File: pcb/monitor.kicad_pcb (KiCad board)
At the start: 4 copper layers, 100 x 100 mm, 146 parts, among them K101 DG128-02P, K102 DG128-02P, K103 DG128-02P, K104 DG128-02P, K105 DG128-02P, K106 DG128-02P, K107 DG128-02P, K108 DG128-02P, K109 DG128-02P, K110 DG128-02P, K111 DG128-02P, K112 DG128-02P, K113 JUMPER_3, K114 JUMPER_3, K3 DG128-02P, K4 DG128-02P, K401 DG128-02P, K402 DG128-02P, K403 DG128-02P, K5 DG128-02P, K6 DG128-02P, K7 CONNECT_2, K8 CONNECT_2, T201 ZUMT718, T202 ZUMT718, T203 ZUMT718, T204 ZUMT718, T205 ZUMT718, T206 ZUMT718, T207 ZUMT718, T208 ZUMT718, T209 ZUMT718, T210 ZUMT718, T211 ZUMT718, T212 ZUMT718, U1 LTC6803-3, U401 ADUM5401

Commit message: Battery connections
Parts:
- moved R219 184.9 mm to (147.3, 111.8), turned to 270 degrees
- moved LD209 181.9 mm to (147.3, 106.7), turned to 180 degrees
- moved T209 178.8 mm to (143.5, 106.7), turned to 270 degrees
- moved D311 177.6 mm to (144.8, 102.9)
- moved R216 176.9 mm to (137.2, 111.8), turned to 270 degrees
- moved R217 176.8 mm to (147.3, 97.8), turned to 270 degrees
- moved LD208 173.8 mm to (137.2, 106.7), turned to 180 degrees
- moved C311 172.6 mm to (142.2, 97.8), turned to 270 degrees
- moved T208 170.8 mm to (133.3, 106.7), turned to 270 degrees
- moved D310 169.4 mm to (134.6, 102.9)
- moved R214 168.5 mm to (137.2, 97.8), turned to 270 degrees
- moved C310 164.3 mm to (132.1, 97.8), turned to 270 degrees
- moved R221 143.6 mm to (111.8, 90.2), turned to 180 degrees
- moved C306 140.5 mm to (111.8, 85.1), turned to 180 degrees
- moved D306 138.1 mm to (106.7, 87.6), turned to 270 degrees
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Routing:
- net /Lowpass/BATT4+: track 0.00 -> 48.4 mm
- net /Lowpass/C7: track 0.00 -> 46.4 mm
- net /Lowpass/C9: track 12.7 -> 55.2 mm
- net /Lowpass/C8: track 6.39 -> 48.3 mm
- net /Lowpass/C4: track 9.06 -> 45.0 mm
- net /Lowpass/BATT6+: track 0.00 -> 26.6 mm
- net /Lowpass/BATT9+: track 0.00 -> 26.6 mm
- net /Lowpass/BATT5+: track 0.00 -> 26.6 mm
- net /Lowpass/BATT7+: track 0.00 -> 26.6 mm
- net /Lowpass/BATT2+: track 0.00 -> 26.0 mm
- net /Lowpass/BATT3+: track 0.00 -> 25.8 mm
- net /Lowpass/BATT8+: track 0.00 -> 25.3 mm
- net /discharge/S7: track 0.00 -> 24.0 mm
- net /Lowpass/C6: track 30.4 -> 52.7 mm
- net AGND: track 41.5 -> 62.7 mm, vias 7 -> 13
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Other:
- net class AGND: clearance 1 -> 0.6

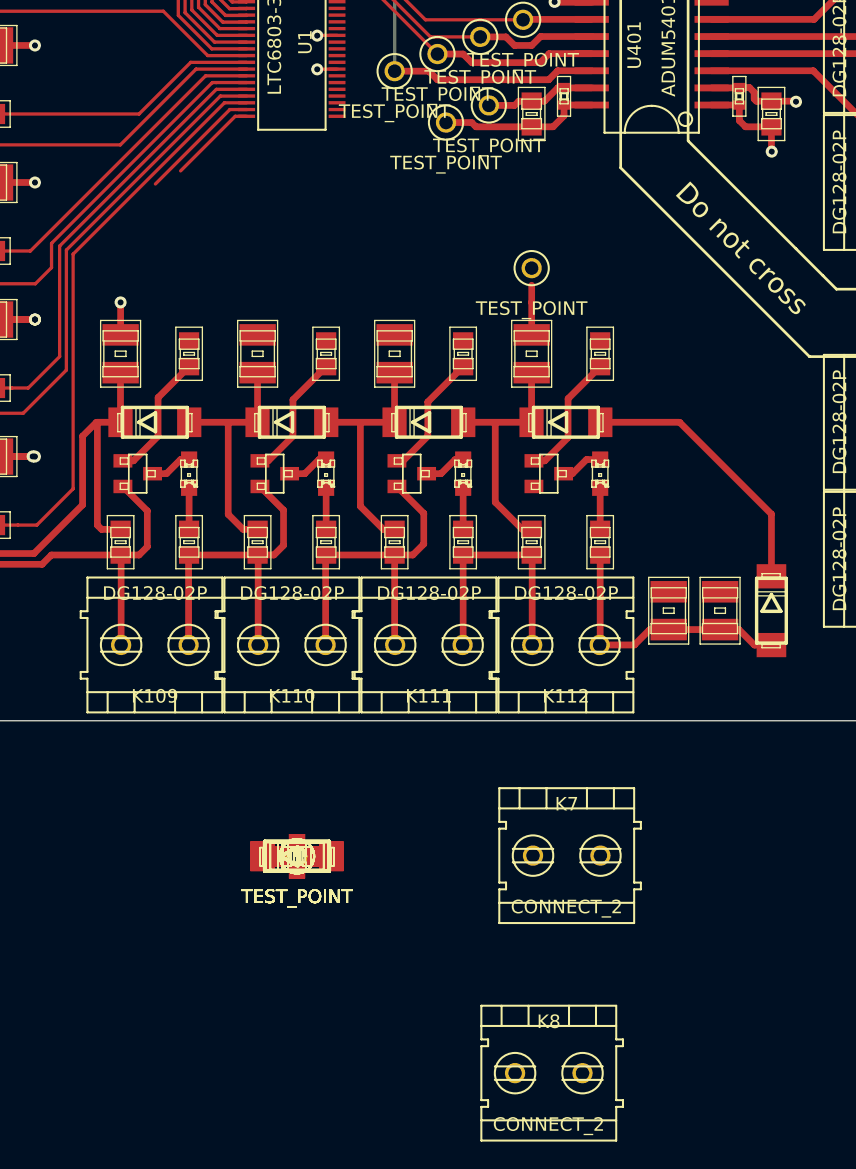
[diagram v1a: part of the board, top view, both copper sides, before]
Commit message: More connections
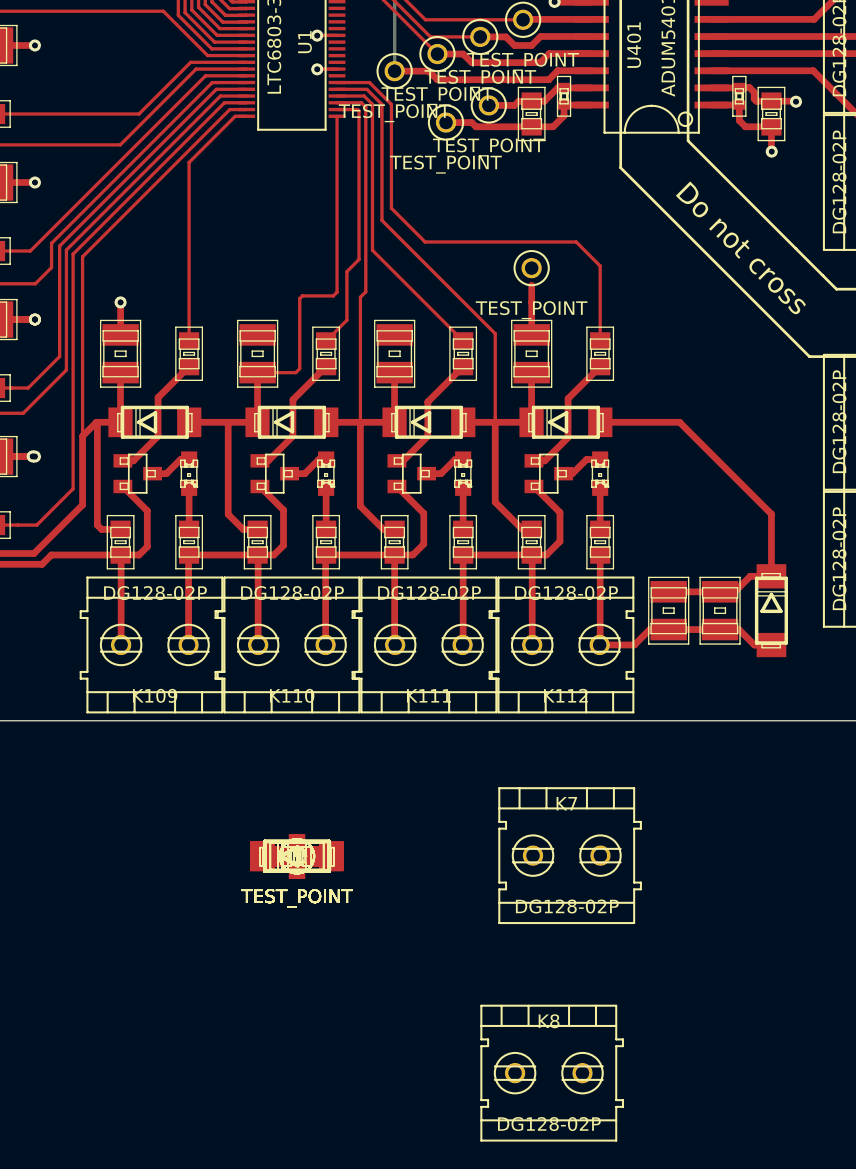
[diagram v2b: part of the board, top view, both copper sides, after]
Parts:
- K7, K8: value CONNECT_2 -> DG128-02P
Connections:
- K113 pad 1: Net-(K113-Pad1) -> DGND
- K113 pad 3: Net-(K113-Pad3) -> /Isolation/5V
- K114 pad 1: Net-(K114-Pad1) -> DGND
- K114 pad 3: Net-(K114-Pad3) -> /Isolation/5V
- K5 pad 1: /Isolation/CSBI -> /Isolation/SDI
- K5 pad 2: /Isolation/SDI -> /Isolation/SCKI
- K6 pad 1: /Isolation/SCKI -> /Isolation/CSBI
- T210 pad E: Net-(T210-PadE) -> (no net)
- T212 pad E: Net-(T212-PadE) -> /Lowpass/BATT1+
- TP111 pad 1: /Isolation/SDI -> /Isolation/SCKI
- TP112 pad 1: /Isolation/CSBI -> /Isolation/SDI
- TP113 pad 1: /Isolation/SCKI -> /Isolation/CSBI
- U1 pad 31: Net-(U1-Pad31) -> (no net)
- U401 pad 7: Net-(U401-Pad7) -> (no net)
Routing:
- net /discharge/S1: track 0.00 -> 35.2 mm
- net /Lowpass/C1: track 18.2 -> 49.1 mm
- net /Lowpass/C2: track 18.2 -> 44.0 mm
- net /Lowpass/C3: track 18.2 -> 42.7 mm
- net /discharge/S2: track 0.00 -> 23.2 mm
- net /Lowpass/C4: track 45.0 -> 65.9 mm
- net /discharge/S3: track 0.00 -> 19.7 mm
- net /discharge/S4: track 6.58 -> 18.9 mm
- net /Lowpass/C0: track 20.1 -> 28.2 mm
- net /Lowpass/BATT1+: track 18.5 -> 25.8 mm
- net Net-(T210-PadE): track 1.24 -> 0.00 mm
- net /Lowpass/BATT8+: track 25.3 -> 26.6 mm

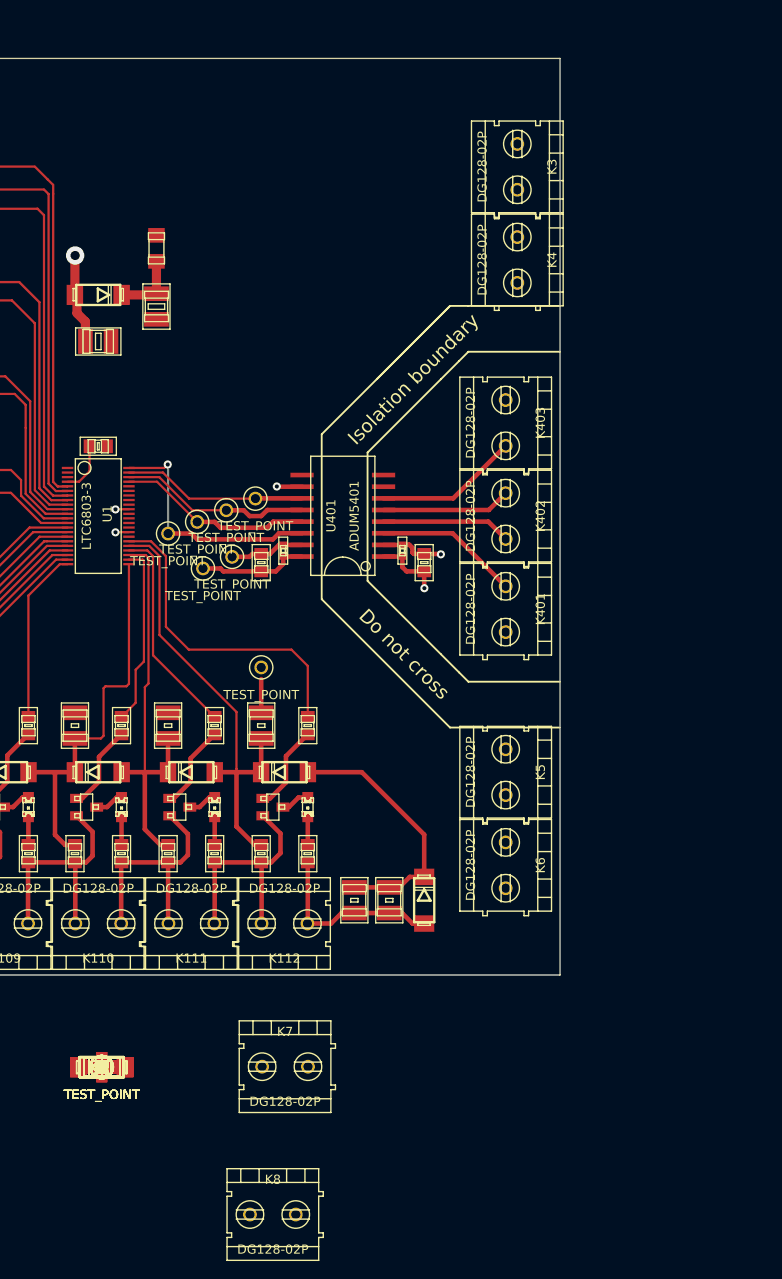
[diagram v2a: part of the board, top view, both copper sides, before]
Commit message: Add temperature connections
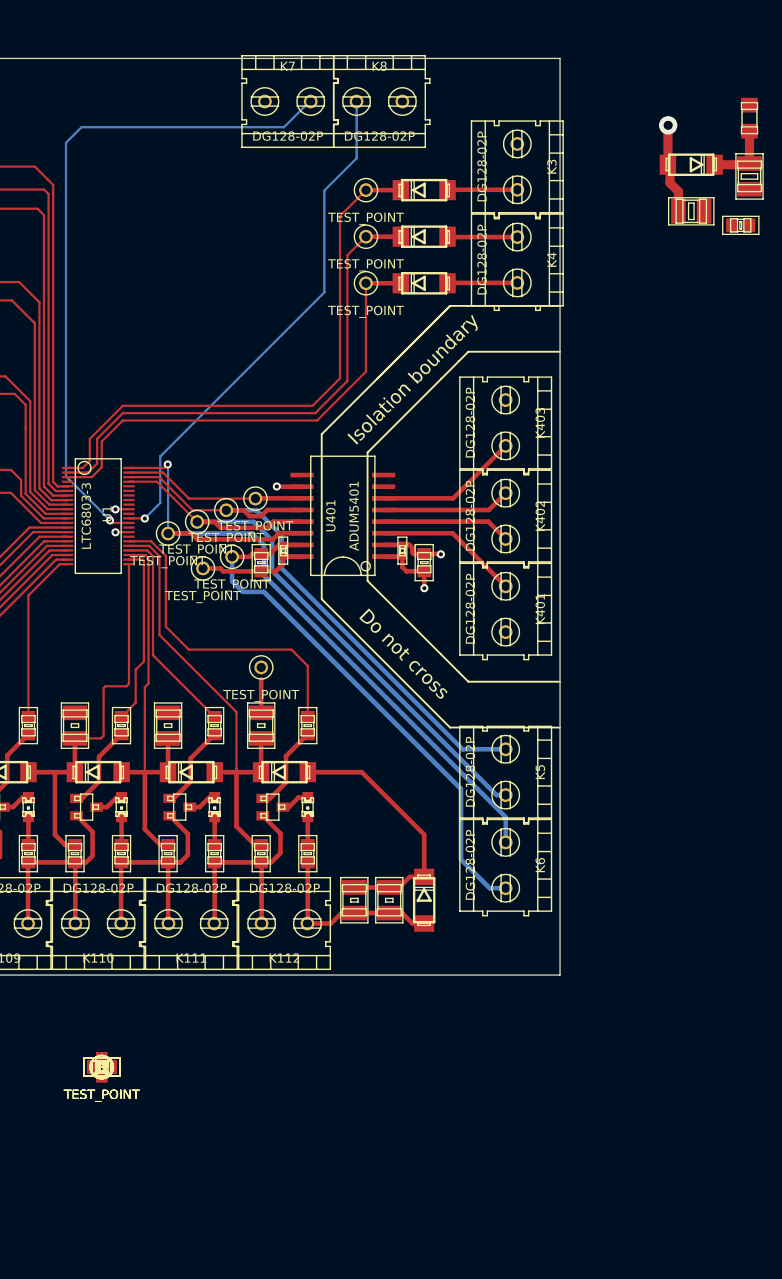
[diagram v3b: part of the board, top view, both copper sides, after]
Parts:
- moved K8 122.0 mm to (165.3, 29.7)
- moved K7 105.3 mm to (155.3, 29.7)
- moved D1 101.9 mm to (170.2, 39.4)
- moved TP108 99.9 mm to (163.8, 39.4)
- moved D2 97.2 mm to (170.2, 44.5)
- moved TP109 95.1 mm to (163.8, 44.5)
- moved D3 92.5 mm to (170.2, 49.5)
- moved TP110 90.2 mm to (163.8, 49.5)
- moved C1 74.1 mm to (204.7, 43.2)
- moved D4 66.2 mm to (199.3, 36.6)
- moved L1 66.2 mm to (205.7, 31.5)
- moved R30 66.2 mm to (199.3, 41.7)
- moved R31 66.2 mm to (205.7, 37.9)
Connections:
- K113 pad 1: DGND -> (no net)
- K113 pad 3: /Isolation/5V -> (no net)
- K114 pad 1: DGND -> (no net)
- K114 pad 3: /Isolation/5V -> (no net)
- K5 pad 1: /Isolation/SDI -> /Isolation/CSBI
- K5 pad 2: /Isolation/SCKI -> /Isolation/SDI
- K6 pad 1: /Isolation/CSBI -> /Isolation/SCKI
- K7 pad 1: /Vtemp1 -> AGND
- K7 pad 2: AGND -> /Vtemp1
- TP111 pad 1: /Isolation/SCKI -> /Isolation/SDI
- TP112 pad 1: /Isolation/SDI -> /Isolation/CSBI
- TP113 pad 1: /Isolation/CSBI -> /Isolation/SCKI
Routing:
- net /Isolation/CSBI: track 27.1 -> 118.8 mm
- net /Vtemp1: track 0.00 -> 73.9 mm, vias 0 -> 1
- net /CSBO: track 0.00 -> 60.7 mm
- net /Vtemp2: track 0.00 -> 56.8 mm, vias 0 -> 1
- net /SDOI: track 0.00 -> 56.6 mm
- net /SCKO: track 0.00 -> 52.4 mm
- net DGND: track 9.67 -> 60.5 mm
- net /Isolation/SCKI: track 21.2 -> 70.9 mm
- net N-0000025: track 0.00 -> 7.63 mm
- net N-0000024: track 0.00 -> 7.63 mm
- net N-0000023: track 0.00 -> 7.63 mm
- net /V+: track 5.60 -> 0.00 mm
- net /Isolation/SDI: track 20.9 -> 25.2 mm

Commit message: First DRC-ok draft
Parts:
- removed TP111, TP112, TP113: TEST_POINT, Aalto_connect:Keystone_Electronics_5000
- C1: footprint oshec_rcl:rcl-C0805 -> oshec_rcl:rcl-C1210
- R30, R31: footprint oshec_rcl:rcl-R1210 -> oshec_rcl:rcl-R0805
- moved D401 183.7 mm to (171.4, 66.0), turned to 90 degrees
- moved K114 142.6 mm to (149.9, 44.5), turned to 90 degrees
- moved K113 140.2 mm to (146.1, 44.5), turned to 90 degrees
- moved R29 97.6 mm to (146.1, 38.1), turned to 270 degrees
- moved R28 97.2 mm to (142.2, 38.1), turned to 270 degrees
- moved L1 94.6 mm to (129.5, 87.6)
- moved R31 88.8 mm to (132.1, 87.6), turned to 270 degrees
- moved D4 85.8 mm to (133.3, 91.4), turned to 0 degrees
- moved R25 82.2 mm to (143.5, 53.3), turned to 270 degrees
- moved R26 81.8 mm to (139.7, 53.3), turned to 270 degrees
- moved R27 81.7 mm to (135.9, 53.3), turned to 270 degrees
- moved C1 81.0 mm to (134.6, 83.8)
- moved R30 78.3 mm to (135.9, 87.6), turned to 270 degrees
- moved LD13 77.1 mm to (143.5, 58.4), turned to 180 degrees
- moved LD14 76.8 mm to (139.7, 58.4), turned to 180 degrees
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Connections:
- K113 pad 1: (no net) -> DGND
- K113 pad 3: (no net) -> /Isolation/5V
- K114 pad 1: (no net) -> DGND
- K114 pad 3: (no net) -> /Isolation/5V
- K5 pad 1: /Isolation/CSBI -> /Isolation/SDI
- K5 pad 2: /Isolation/SDI -> /Isolation/SCKI
- K6 pad 1: /Isolation/SCKI -> /Isolation/CSBI
- T210 pad E: (no net) -> /Lowpass/BATT8+
- U1 pad 31: (no net) -> Net-(U1-Pad31)
- U401 pad 7: (no net) -> Net-(U401-Pad7)
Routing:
- net /Vref: track 0.00 -> 42.8 mm, vias 0 -> 2
- net /TOS: track 0.00 -> 42.4 mm, vias 0 -> 1
- net /Lowpass/C0: track 28.2 -> 69.7 mm
- net /Isolation/SDI: track 25.2 -> 64.3 mm
- net /Isolation/CSBI: track 118.8 -> 81.4 mm
- net /VMODE: track 0.00 -> 35.8 mm, vias 0 -> 1
- net /WDTB: track 0.00 -> 18.6 mm, vias 0 -> 2
- net /GPIO2: track 0.00 -> 18.2 mm, vias 0 -> 2
- net /GPIO1: track 0.00 -> 18.2 mm, vias 0 -> 2
- net /V+: track 0.00 -> 17.5 mm
- net /Vtemp1: track 73.9 -> 56.7 mm, vias 1 -> 2
- net /Isolation/5V: track 16.3 -> 32.4 mm, vias 2 -> 3
- net DGND: track 60.5 -> 76.0 mm, vias 1 -> 2
- net Net-(LD15-PadA): track 0.00 -> 3.08 mm
- net Net-(LD14-PadA): track 0.00 -> 3.08 mm
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- added copper zone on F.Cu, net /Isolation/GND1
- added copper zone on Inner2.Cu, net /Isolation/GND1
- added copper zone on Inner1.Cu, net /Isolation/Vin
- added copper zone on Inner1.Cu, net /discharge/BATT12+
- added copper zone on Inner2.Cu, net AGND
- added copper zone on F.Cu, net DGND
- added copper zone on Inner2.Cu, net DGND

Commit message: Implement changes
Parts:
- removed K3, K4, K402, K403, K5, K6: DG128-02P, Aalto_connect:CONNECT_2_5.00mm_SCREW_DG128-02P_DG128-5.0-02P-14-00A(H)
- added K115: MOUNT, Aalto_connect:M3_MOUNT_BARE, F.Cu at (88.0, 28.0)
- added K116: MOUNT, Aalto_connect:M3_MOUNT_BARE, F.Cu at (88.0, 122.0)
- added K117: MOUNT, Aalto_connect:M3_MOUNT_BARE, F.Cu at (182.0, 28.0)
- added K118: MOUNT, Aalto_connect:M3_MOUNT_BARE, F.Cu at (182.0, 122.0)
- added K119: MOUNT, Aalto_connect:M3_MOUNT_BARE, F.Cu at (163.0, 28.0)
- added K120: CONNECT_4, Aalto_connect:2_54_MM_HEADER_4, F.Cu at (172.0, 28.0)
- added K121: CONNECT_4, Aalto_connect:2_54_MM_HEADER_4, F.Cu at (172.0, 122.0)
- added K122: MOUNT, Aalto_connect:M3_MOUNT_BARE, F.Cu at (163.0, 122.0)
- added TP111: TEST_POINT, Aalto_connect:Keystone_Electronics_5000, F.Cu at (163.8, 34.3)
- C1, R313: footprint oshec_rcl:rcl-C1210 -> oshec_rcl:rcl-C0805
- K401: value DG128-02P -> CONNECT_6; footprint Aalto_connect:CONNECT_2_5.00mm_SCREW_DG128-02P_DG128-5.0-02P-14-00A(H) -> Aalto_connect:2_54_MM_HEADER_6
- K7, K8: footprint Aalto_connect:CONNECT_2_5.00mm_SCREW_DG128-02P_DG128-5.0-02P-14-00A(H) -> Aalto_connect:CONNECT_2_2mm54_VERT
- LD201, LD202, LD203, LD204, LD205, LD206, LD207, LD208, LD209, LD210, LD211, LD212: footprint oshec_led:led-CHIPLED_0805 -> oshec_led:led-CHIP-LED0805
- moved D3 16.5 mm to (176.5, 34.3), turned to 90 degrees
- moved D313 13.1 mm to (163.8, 105.4), turned to 0 degrees
- moved K8 10.8 mm to (142.2, 38.1), turned to 180 degrees
- moved D2 10.5 mm to (172.7, 34.3), turned to 90 degrees
- moved K401 10.5 mm to (181.6, 74.9)
- moved C313 8.52 mm to (162.6, 109.2), turned to 180 degrees
- moved K7 8.52 mm to (135.9, 38.1), turned to 180 degrees
- moved R28 6.35 mm to (137.2, 41.9), turned to 0 degrees
- moved R29 6.35 mm to (141.0, 41.9), turned to 180 degrees
- moved D1 5.24 mm to (168.9, 34.3), turned to 90 degrees
- moved R313 3.81 mm to (162.6, 113.0), turned to 0 degrees
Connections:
- K401 pad 1: /Isolation/CS -> /Isolation/GND1
- K401 pad 2: /Isolation/Vin -> /Isolation/MISO
- K7 pad 1: AGND -> DGND
- K8 pad 2: AGND -> DGND
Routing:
- net /V+: track 17.5 -> 89.2 mm
- net DGND: track 76.0 -> 26.2 mm, vias 2 -> 3
- net /Vtemp2: track 57.4 -> 90.8 mm
- net AGND: track 65.6 -> 85.2 mm
- net /Isolation/SCKI: track 69.2 -> 88.7 mm
- net /SCKO: track 52.4 -> 69.9 mm
- net /Isolation/SDI: track 64.3 -> 80.3 mm
- net /Lowpass/C0: track 69.7 -> 54.9 mm
- net /discharge/BATT12+: track 17.4 -> 30.2 mm
- net /Vtemp1: track 56.7 -> 46.4 mm
- net /SDOI: track 56.6 -> 66.7 mm
- net /Isolation/CSBI: track 81.4 -> 89.4 mm
- net Net-(D2-PadA): track 7.63 -> 3.97 mm
- net Net-(D3-PadA): track 7.63 -> 4.04 mm
- net /CSBO: track 60.7 -> 64.0 mm
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
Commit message: Finishing touches
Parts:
- C1: footprint oshec_rcl:rcl-C0805 -> oshec_rcl:rcl-C1210
- U1: footprint Aalto_ic:SSOP44 -> Aalto_ic:SSOP44_HS
- moved TP106 0.43 mm to (142.6, 76.6)
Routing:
- net /Lowpass/C9: track 55.2 -> 45.3 mm
- net /Lowpass/C10: track 65.3 -> 57.7 mm
- net /Lowpass/C11: track 74.6 -> 67.8 mm
- net /Lowpass/C8: track 48.3 -> 42.7 mm
- net /Lowpass/C4: track 65.9 -> 61.7 mm
- net /Vref: track 42.8 -> 46.7 mm
- net /V+: track 89.2 -> 91.9 mm
- net /discharge/S12: track 50.8 -> 48.7 mm
- net /Lowpass/C6: track 52.7 -> 50.8 mm
- net /Lowpass/C7: track 46.4 -> 44.7 mm
- net /discharge/S7: track 24.0 -> 25.7 mm
- net /Lowpass/C5: track 58.1 -> 59.7 mm
- net /discharge/S9: track 21.9 -> 20.4 mm
- net /discharge/S6: track 32.6 -> 34.0 mm
- net /Lowpass/C12: track 71.1 -> 70.0 mm
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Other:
- board text added: "!MCU"
- board text added: "!TOS"
- board text added: "10- 9+"
- board text added: "11- 10+"
- board text added: "12- 11+"
- board text added: "2- 1+"
- board text added: "3- 2+"
- board text added: "4- 3+"
- board text added: "6- 5+"
- board text added: "7- 6+"
- board text added: "8- 7+"
- board text added: "9- 8+"
- board text added: "Battery 1 -"
- board text added: "Battery 12 +"
- board text added: "Battery 4+"
- board text added: "Battery 5 -"
- board text added: "CS"
- board text added: "CSBI"
- board text added: "CSBO"
- board text added: "DGND"
- board text added: "GND"
- board text added: "GP1"
- board text added: "GP2"
- board text added: "MCU"
- board text added: "MISO"
- board text added: "MOSI"
- board text added: "SCKI"
- board text added: "SCKO"
- board text added: "SCL"
- board text added: "SDI"
- board text added: "SDOI"
- board text added: "TOS"
- board text added: "Temp1"
- board text added: "Temp2"
- board text added: "V+"
- board text added: "Vin"
- board text added: "Watchdog"
